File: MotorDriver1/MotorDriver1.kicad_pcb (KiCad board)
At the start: 4 copper layers, 72 x 76 mm, 76 parts, among them IC1 STM32C092RCT6, J1 GT-USB-7010ASV, J2 Conn_01x02, J3 Conn_01x02, Q1 IRLZ44NSTRLPBF, Q2 IRLZ44NSTRLPBF, Q3 IRLZ44NSTRLPBF, Q4 IRLZ44NSTRLPBF, SW1 K2-6639SP-C4SC-04, SW2 K2-6639SP-C4SC-04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

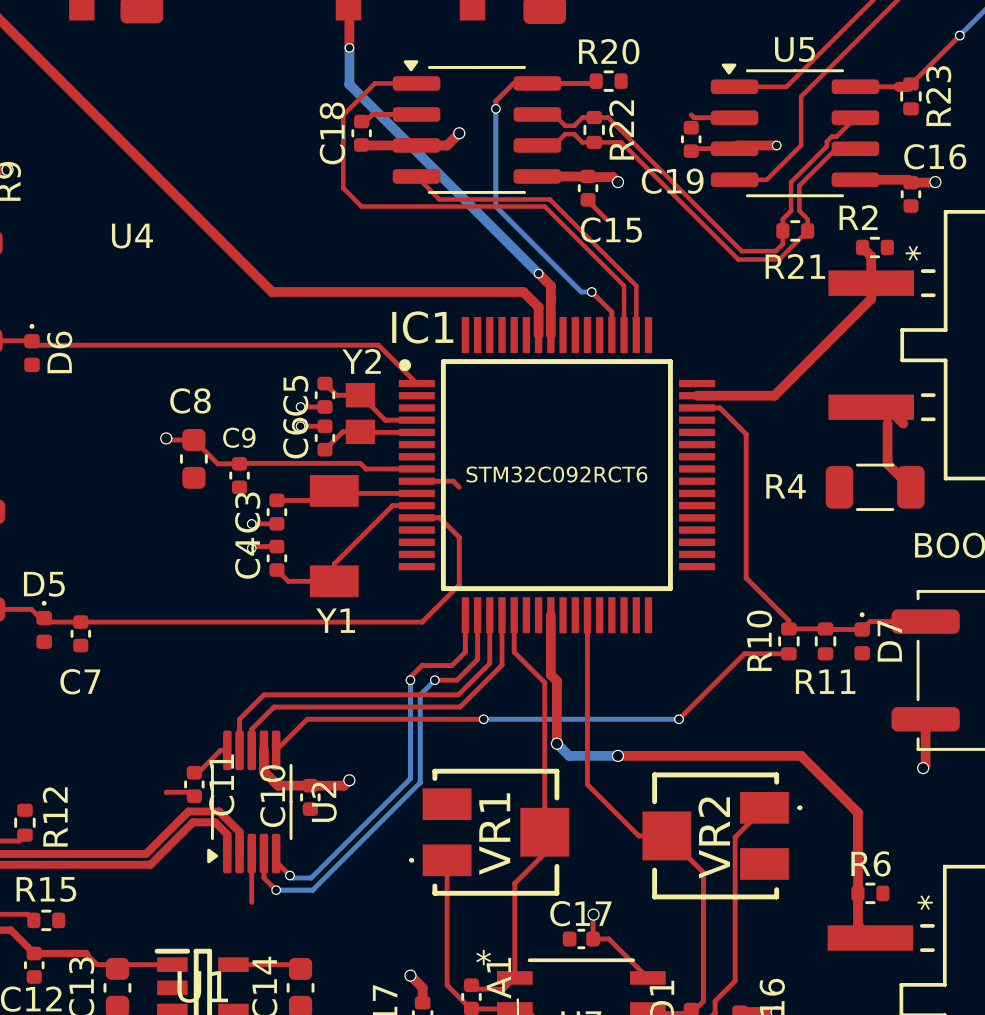
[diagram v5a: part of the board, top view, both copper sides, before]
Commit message: Tuned skew
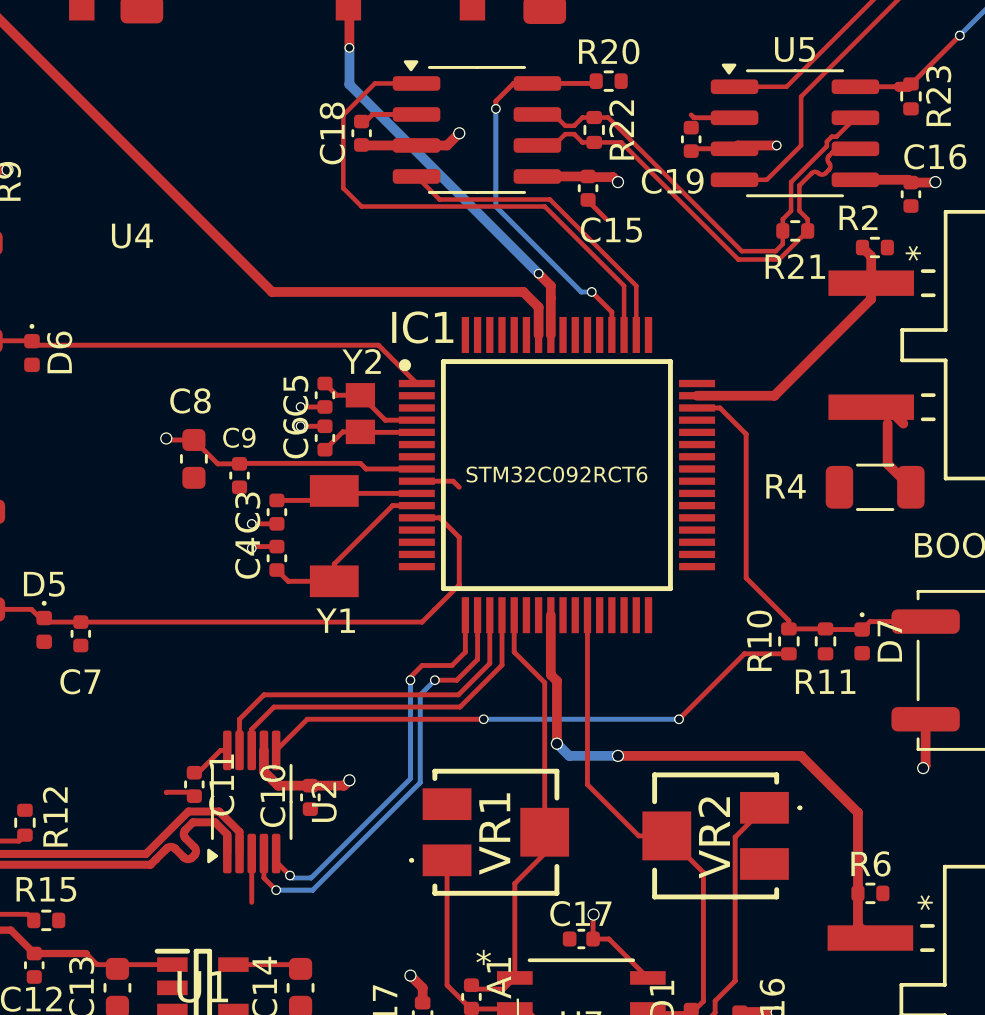
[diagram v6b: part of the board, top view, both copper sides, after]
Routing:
- net USB_D+: track 14.0 -> 15.5 mm
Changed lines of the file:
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@@
+	)
+	(segment
+		(start 138.5 109)
+		(end 138.5 108.22145)
+		(width 0.328)
+		(layer "F.Cu")
+		(net 69)
 	)
 	(segment
@@
 	)
 	(segment
+		(start 137.150553 109.07684)
+		(end 137.065702 109.161692)
+		(width 0.328)
+		(layer "F.Cu")
+		(net 69)
+	)
+	(segment
+		(start 136.019183 108.793998)
+		(end 135.934329 108.87885)
+		(width 0.328)
+		(layer "F.Cu")
+		(net 69)
+	)
+	(segment
+		(start 135.579092 109.234086)
+		(end 135.35383 109.459348)
+		(width 0.328)
+		(layer "F.Cu")
+		(net 69)
+	)
+	(segment
+		(start 135.934329 108.87885)
+		(end 135.579092 109.234086)
+		(width 0.328)
+		(layer "F.Cu")
+		(net 69)
+	)
+	(segment
+		(start 129 110.316799)
+		(end 129 109.513399)
+		(width 0.328)
+		(layer "F.Cu")
+		(net 69)
+	)
+	(segment
+		(start 129 109.513399)
+		(end 128.9745 109.487899)
+		(width 0.328)
+		(layer "F.Cu")
+		(net 69)
+	)
+	(segment
+		(start 136.72629 109.161692)
+		(end 136.358595 108.793997)
+		(width 0.328)
+		(layer "F.Cu")
+		(net 69)
+	)
+	(segment
+		(start 128.828899 110.4879)
+		(end 129 110.316799)
+		(width 0.328)
+		(layer "F.Cu")
+		(net 69)
+	)
+	(segment
+		(start 136.782858 108.369732)
+		(end 137.150554 108.737428)
+		(width 0.328)
+		(layer "F.Cu")
+		(net 69)
+	)
+	(segment
+		(start 128.9745 109.487899)
+		(end 128.075 109.487899)
+		(width 0.328)
+		(layer "F.Cu")
+		(net 69)
+	)
+	(segment
+		(start 138 107.72145)
+		(end 137.091728 107.72145)
+		(width 0.328)
+		(layer "F.Cu")
+		(net 69)
+	)
+	(segment
+		(start 137.091728 107.72145)
+		(end 136.782858 108.03032)
+		(width 0.328)
+		(layer "F.Cu")
+		(net 69)
+	)
+	(segment
 		(start 138.5 108.22145)
 		(end 138 107.72145)
@@
 	)
 	(segment
-		(start 129 110.316799)
-		(end 129 109.513399)
-		(width 0.328)
-		(layer "F.Cu")
-		(net 69)
-	)
-	(segment
-		(start 129 109.513399)
-		(end 128.9745 109.487899)
-		(width 0.328)
-		(layer "F.Cu")
-		(net 69)
-	)
-	(segment
-		(start 128.828899 110.4879)
-		(end 129 110.316799)
-		(width 0.328)
-		(layer "F.Cu")
-		(net 69)
-	)
-	(segment
-		(start 137.091728 107.72145)
-		(end 135.35383 109.459348)
-		(width 0.328)
-		(layer "F.Cu")
-		(net 69)
-	)
-	(segment
-		(start 128.9745 109.487899)
-		(end 128.075 109.487899)
-		(width 0.328)
-		(layer "F.Cu")
-		(net 69)
-	)
-	(segment
-		(start 138 107.72145)
-		(end 137.091728 107.72145)
-		(width 0.328)
-		(layer "F.Cu")
-		(net 69)
-	)
-	(segment
-		(start 138.5 109)
-		(end 138.5 108.22145)
-		(width 0.328)
-		(layer "F.Cu")
-		(net 69)
-	)
-	(segment
 		(start 128.075 110.4879)
 		(end 128.828899 110.4879)
+		(width 0.328)
+		(layer "F.Cu")
+		(net 69)
+	)
+	(arc
+		(start 136.358595 108.793997)
+		(mid 136.188889 108.723703)
+		(end 136.019183 108.793998)
+		(width 0.328)
+		(layer "F.Cu")
+		(net 69)
+	)
+	(arc
+		(start 137.150554 108.737428)
+		(mid 137.220849 108.907133)
+		(end 137.150553 109.07684)
+		(width 0.328)
+		(layer "F.Cu")
+		(net 69)
+	)
+	(arc
+		(start 137.065702 109.161692)
+		(mid 136.895995 109.231988)
+		(end 136.72629 109.161692)
+		(width 0.328)
+		(layer "F.Cu")
+		(net 69)
+	)
+	(arc
+		(start 136.782858 108.03032)
+		(mid 136.712562 108.200027)
+		(end 136.782858 108.369732)
 		(width 0.328)
 		(layer "F.Cu")
@@
 	)
 	(segment
+		(start 162.99992 81.138011)
+		(end 163.141341 80.996589)
+		(width 0.186)
+		(layer "F.Cu")
+		(net 118)
+	)
+	(segment
 		(start 151.875 80)
 		(end 152.3395 79.5355)
@@
 	)
 	(segment
+		(start 162.27 83.019999)
+		(end 161.9305 82.680499)
+		(width 0.186)
+		(layer "F.Cu")
+		(net 118)
+	)
+	(segment
+		(start 163.437247 80.135)
+		(end 164.225 80.135)
+		(width 0.186)
+		(layer "F.Cu")
+		(net 118)
+	)
+	(segment
+		(start 153.044999 79.875)
+		(end 153.525 79.875)
+		(width 0.186)
+		(layer "F.Cu")
+		(net 118)
+	)
+	(segment
+		(start 161.9305 81.641747)
+		(end 162.434236 81.138011)
+		(width 0.186)
+		(layer "F.Cu")
+		(net 118)
+	)
+	(segment
+		(start 161.9305 82.680499)
+		(end 161.9305 81.641747)
+		(width 0.186)
+		(layer "F.Cu")
+		(net 118)
+	)
+	(segment
+		(start 152.3395 79.5355)
+		(end 152.705499 79.5355)
+		(width 0.186)
+		(layer "F.Cu")
+		(net 118)
+	)
+	(segment
+		(start 163.282764 80.289482)
+		(end 163.437247 80.135)
+		(width 0.186)
+		(layer "F.Cu")
+		(net 118)
+	)
+	(segment
+		(start 152.705499 79.5355)
+		(end 153.044999 79.875)
+		(width 0.186)
+		(layer "F.Cu")
+		(net 118)
+	)
+	(segment
+		(start 161.0995 84.6705)
+		(end 159.429376 84.6705)
+		(width 0.186)
+		(layer "F.Cu")
+		(net 118)
+	)
+	(segment
 		(start 162.27 83.5)
 		(end 162.27 83.019999)
@@
 	)
 	(segment
-		(start 153.044999 79.875)
-		(end 153.525 79.875)
-		(width 0.186)
-		(layer "F.Cu")
-		(net 118)
-	)
-	(segment
-		(start 152.3395 79.5355)
-		(end 152.705499 79.5355)
-		(width 0.186)
-		(layer "F.Cu")
-		(net 118)
-	)
-	(segment
-		(start 152.705499 79.5355)
-		(end 153.044999 79.875)
-		(width 0.186)
-		(layer "F.Cu")
-		(net 118)
-	)
-	(segment
-		(start 161.9305 82.680499)
-		(end 161.9305 81.641747)
-		(width 0.186)
-		(layer "F.Cu")
-		(net 118)
-	)
-	(segment
-		(start 161.0995 84.6705)
-		(end 159.429376 84.6705)
-		(width 0.186)
-		(layer "F.Cu")
-		(net 118)
-	)
-	(segment
-		(start 162.27 83.019999)
-		(end 161.9305 82.680499)
-		(width 0.186)
-		(layer "F.Cu")
-		(net 118)
-	)
-	(segment
-		(start 161.9305 81.641747)
-		(end 163.437247 80.135)
-		(width 0.186)
-		(layer "F.Cu")
-		(net 118)
-	)
-	(segment
 		(start 151.2 80)
 		(end 151.875 80)
@@
 	)
 	(segment
-		(start 163.437247 80.135)
-		(end 164.225 80.135)
+		(start 163.141341 80.430903)
+		(end 163.282764 80.289482)
+		(width 0.186)
+		(layer "F.Cu")
+		(net 118)
+	)
+	(arc
+		(start 163.141341 80.713746)
+		(mid 163.082762 80.572325)
+		(end 163.141341 80.430903)
+		(width 0.186)
+		(layer "F.Cu")
+		(net 118)
+	)
+	(arc
+		(start 162.717078 81.138011)
+		(mid 162.858499 81.196589)
+		(end 162.99992 81.138011)
+		(width 0.186)
+		(layer "F.Cu")
+		(net 118)
+	)
+	(arc
+		(start 163.141341 80.996589)
+		(mid 163.19992 80.855167)
+		(end 163.141341 80.713746)
+		(width 0.186)
+		(layer "F.Cu")
+		(net 118)
+	)
+	(arc
+		(start 162.434236 81.138011)
+		(mid 162.575657 81.079433)
+		(end 162.717078 81.138011)
 		(width 0.186)
 		(layer "F.Cu")
@@
 		)
 	)
+	(generated
+		(type tuning_pattern)
+		(name "Tuning Pattern")
+		(layer "F.Cu")
+		(base_line
+			(pts
+				(xy 162.434236 81.138011) (xy 163.437247 80.135) (xy 164.225 80.135)
+			)
+		)
+		(base_line_coupled
+			(pts
+				(xy 162.193113 80.896887) (xy 162.185305 80.904695)
+			)
+		)
+		(corner_radius_percent 80)
+		(end
+			(xy 164.225 80.135)
+		)
+		(initial_side "right")
+		(last_diff_pair_gap 0.18)
+		(last_netname "/FDCAN/CAN_N")
+		(last_status "too_short")
+		(last_track_width 0.186)
+		(last_tuning "-0.6660 mm (too short)")
+		(max_amplitude 1)
+		(min_amplitude 0.2)
+		(min_spacing 0.6)
+		(origin
+			(xy 162.434236 81.138011)
+		)
+		(override_custom_rules no)
+		(rounded yes)
+		(single_sided no)
+		(target_length 1000000)
+		(target_length_max 1000000)
+		(target_length_min 0)
+		(target_skew 0)
+		(target_skew_max 0.1)
+		(target_skew_min -0.1)
+		(tuning_mode "diff_pair_skew")
+		(members "07ad427e-7fa2-4564-bc98-efe5c55014bd" "34c19e6f-b550-4b47-9d7c-764e2c5222b6"
+			"60646e0d-f95d-4ff2-8d1c-084e9fa1986a" "68a9b316-4c4d-45fc-b123-c2fbf42771f2"
+			"c874d229-3baf-4292-aa64-e2e76c0fbd7f" "d0e06409-6693-41f3-81db-6bec335d477b"
+			"e5fdd4c5-7866-45bc-a402-c1bd07c12c57" "f9fedb3f-2a56-4460-ac0a-20e2dbbeaecb"
+		)
+	)
+	(generated
+		(type tuning_pattern)
+		(name "Tuning Pattern")
+		(layer "F.Cu")
+		(base_line
+			(pts
+				(xy 136.782858 108.03032) (xy 135.579092 109.234086)
+			)
+		)
+		(base_line_coupled
+			(pts
+				(xy 136.46968 107.717142) (xy 136.478098 107.708724)
+			)
+		)
+		(corner_radius_percent 80)
+		(end
+			(xy 135.579092 109.234086)
+		)
+		(initial_side "left")
+		(last_diff_pair_gap 0.18)
+		(last_netname "USB_D+")
+		(last_status "tuned")
+		(last_track_width 0.328)
+		(last_tuning "-0.0690 mm (tuned)")
+		(max_amplitude 1)
+		(min_amplitude 0.2)
+		(min_spacing 0.6)
+		(origin
+			(xy 136.782858 108.03032)
+		)
+		(override_custom_rules no)
+		(rounded yes)
+		(single_sided no)
+		(target_length 1000000)
+		(target_length_max 1000000)
+		(target_length_min 0)
+		(target_skew 0)
+		(target_skew_max 0.1)
+		(target_skew_min -0.1)
+		(tuning_mode "diff_pair_skew")
+		(members "346360f9-c97c-4d49-9543-b53220254f6f" "37ef3dae-c240-4d05-8e29-bdc625f8a2d3"
+			"5a26d633-af63-4b50-b7dd-8654f7730032" "77570f47-4b12-4505-ab93-47f28767675f"
+			"7c5abc31-6362-4851-8dd7-dcea5feca7f9" "81609057-4e88-4c36-8b6a-16488d123649"
+			"88160bae-1a1c-4e96-8806-a09707b074ea" "a8df8d61-1616-49e8-87f6-0271276a45e5"
+			"d4071b8f-e833-4120-bce4-8a8323d37e6a"
+		)
+	)

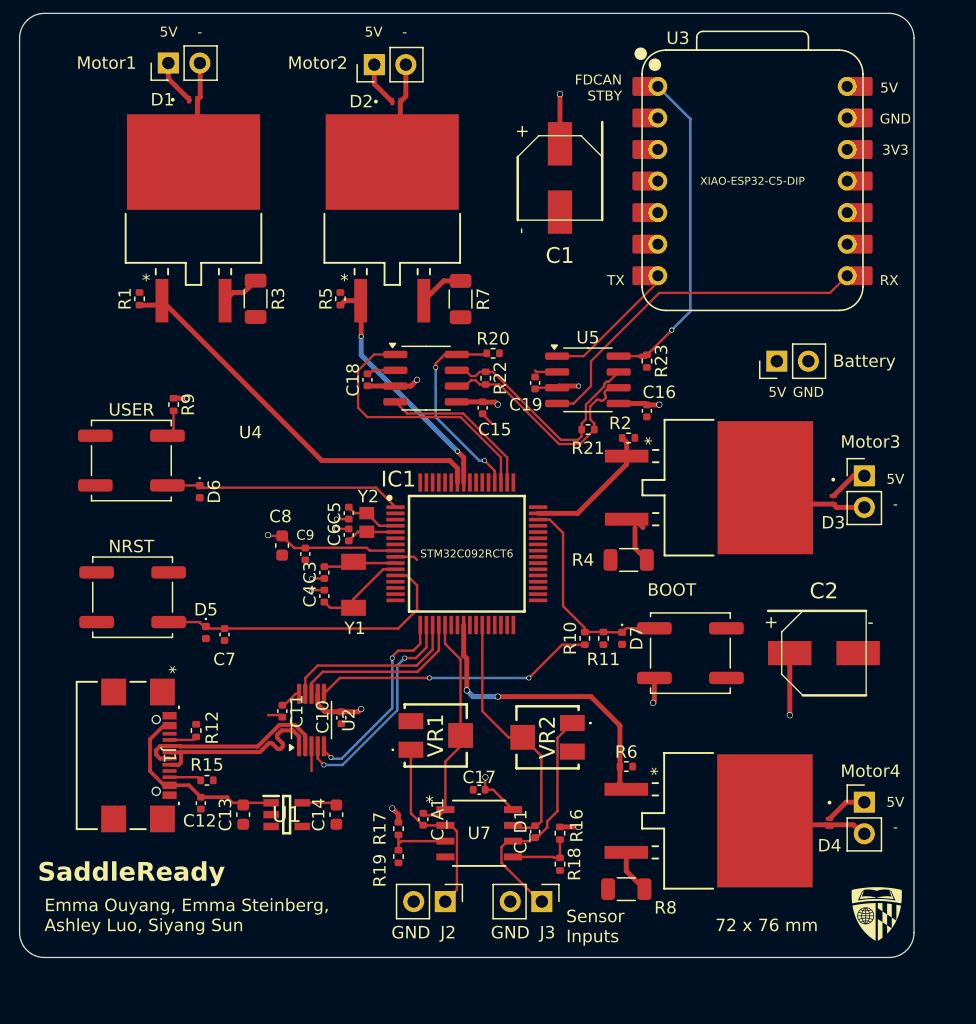
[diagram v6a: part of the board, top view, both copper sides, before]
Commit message: Added tooling holes
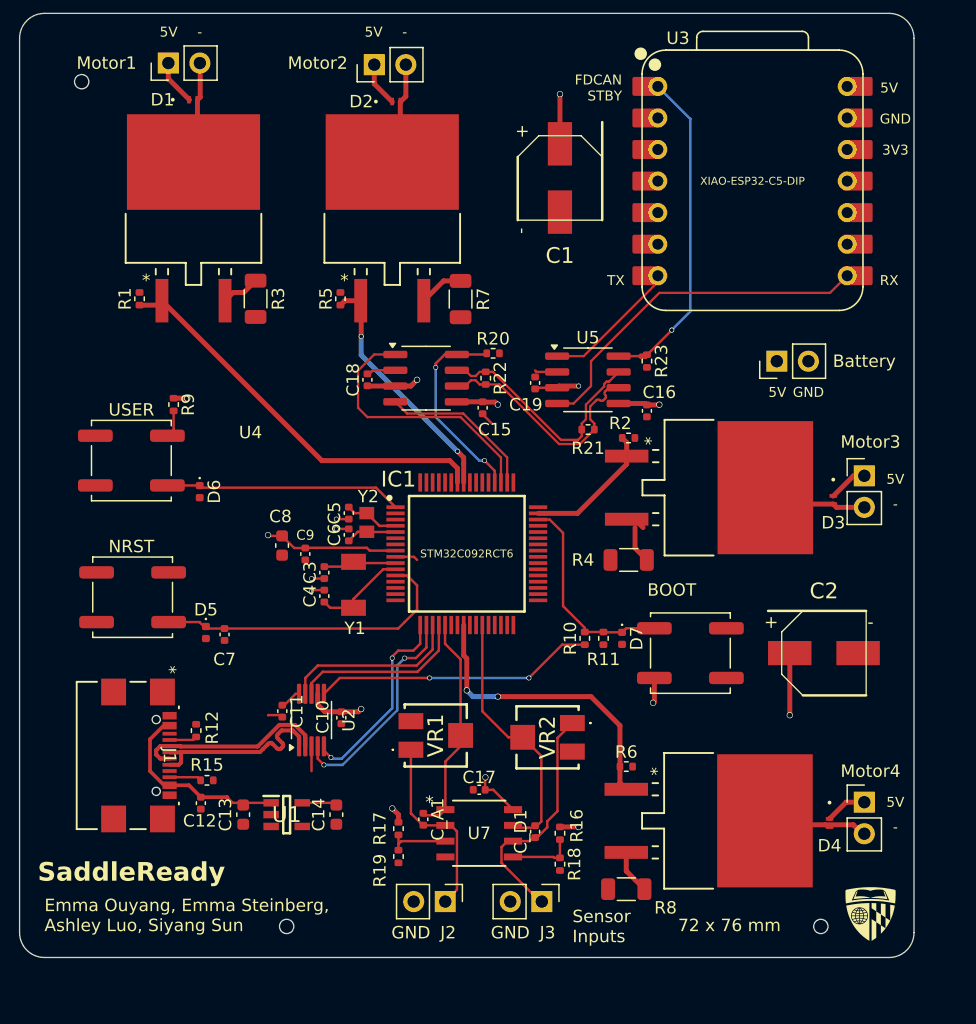
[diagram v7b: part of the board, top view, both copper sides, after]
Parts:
- added H1: MountingHole, MountingHole:ToolingHole_1.152mm, F.Cu at (121.0, 55.5)
- added H2: MountingHole, MountingHole:ToolingHole_1.152mm, F.Cu at (137.5, 123.5)
- added H3: MountingHole, MountingHole:ToolingHole_1.152mm, F.Cu at (180.5, 123.5)
- moved G*** 0.50 mm to (184.5, 122.5)
